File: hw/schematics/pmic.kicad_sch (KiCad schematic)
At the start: 40 parts, among them J1 TYPE-C-31-M-13C, J2 S2B-PH-SM4-TB, U1 NPM1300-QEAA-R

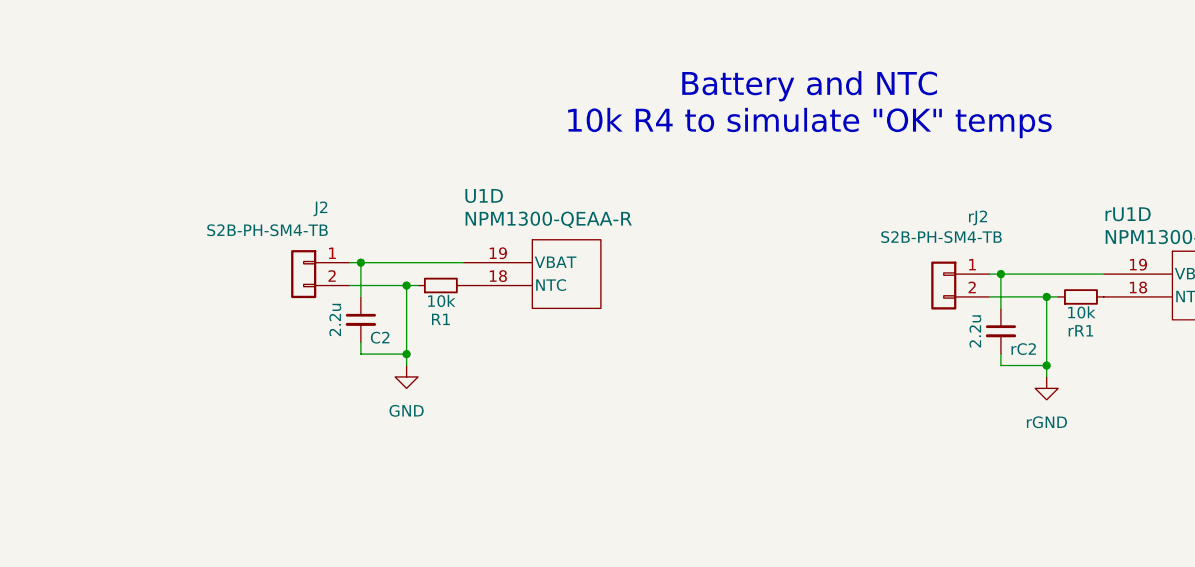
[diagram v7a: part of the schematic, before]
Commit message: Fix missing pads
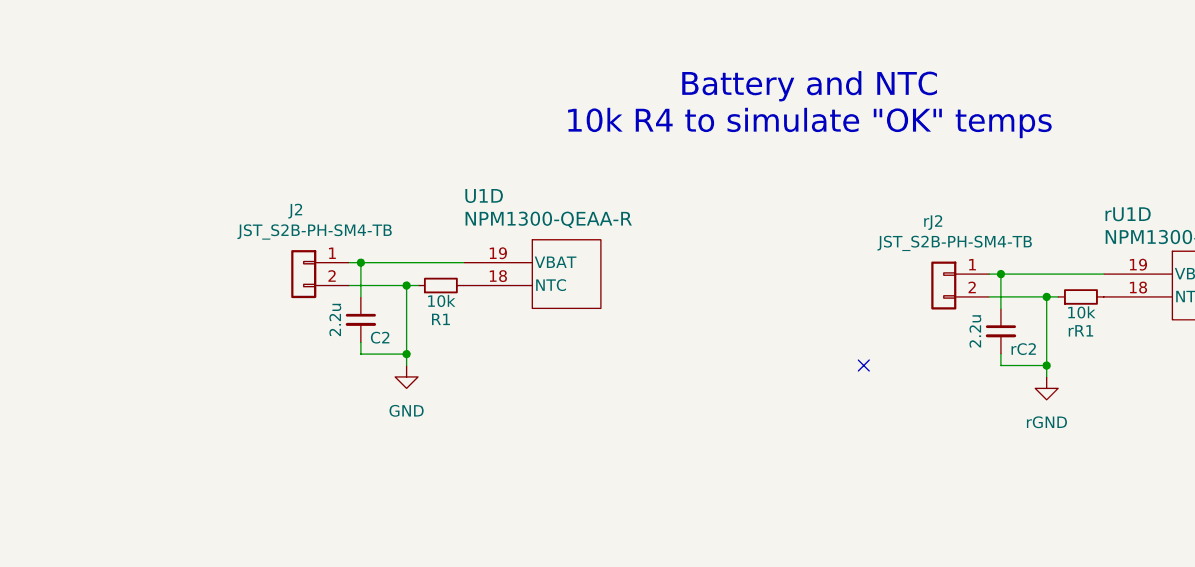
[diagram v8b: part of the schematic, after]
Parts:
- removed J2, rJ2: S2B-PH-SM4-TB, Alidade:JST_S2B-PH-SM4-TB, symbol Alidade:Conn_01x02
- added J2, rJ2: JST_S2B-PH-SM4-TB, Alidade:JST_S2B-PH-SM4-TB, symbol Alidade:JST_S2B-PH-SM4-TB
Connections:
- net GND: now also J2.2 (Pin_2)
- net rGND: now also rJ2.2 (Pin_2)
- net at C2.1, U1.19 (VBAT): now also J2.1 (Pin_1)
- net at rC2.1, rU1.19 (VBAT): now also rJ2.1 (Pin_1)
- no-connect marks 24 -> 25
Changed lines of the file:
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@@
 	)
 	(no_connect
+		(at 332.74 77.47)
+	)
+	(no_connect
 		(at 76.2 67.31)
 	)
@@
 	)
 	(symbol
-		(lib_id "Alidade:Conn_01x02")
-		(at 270.51 66.04 0)
-		(mirror y)
-		(unit 1)
-		(exclude_from_sim no)
-		(in_bom yes)
-		(on_board yes)
-		(dnp no)
-		(property "Reference" "J2"
-			(at 273.304 59.944 0)
-			(effects
-				(font
-					(size 1.27 1.27)
-				)
-				(justify left)
-			)
-		)
-		(property "Value" "S2B-PH-SM4-TB"
-			(at 273.304 62.484 0)
-			(effects
-				(font
-					(size 1.27 1.27)
-				)
-				(justify left)
-			)
-		)
-		(property "Footprint" "Alidade:JST_S2B-PH-SM4-TB"
-			(at 270.51 66.04 0)
-			(effects
-				(font
-					(size 1.27 1.27)
-				)
-				(hide yes)
-			)
-		)
-		(property "Datasheet" "~"
-			(at 270.51 66.04 0)
-			(effects
-				(font
-					(size 1.27 1.27)
-				)
-				(hide yes)
-			)
-		)
-		(property "Description" "Generic connector, single row, 01x02"
-			(at 268.224 58.674 0)
-			(effects
-				(font
-					(size 1.27 1.27)
-				)
-				(hide yes)
-			)
-		)
-		(property "LCSC Part #" "C295747"
-			(at 270.51 66.04 0)
-			(effects
-				(font
-					(size 1.27 1.27)
-				)
-				(hide yes)
-			)
-		)
-		(pin "2"
-		)
-		(pin "1"
-		)
-		(instances
-			(project "alidade"
-				(path "/4cc5d416-57f5-4147-8183-e03ae6b1198a/29a12dcc-0491-44a2-8290-cbef7c573a8c"
-					(reference "J2")
-					(unit 1)
-				)
-			)
-		)
-	)
-	(symbol
 		(lib_id "Alidade:rAVDD")
 		(at 176.53 140.97 0)
@@
 	)
 	(symbol
+		(lib_id "Alidade:JST_S2B-PH-SM4-TB")
+		(at 341.63 67.31 0)
+		(mirror y)
+		(unit 1)
+		(exclude_from_sim no)
+		(in_bom yes)
+		(on_board yes)
+		(dnp no)
+		(property "Reference" "rJ2"
+			(at 341.63 61.468 0)
+			(effects
+				(font
+					(size 1.27 1.27)
+				)
+				(justify left)
+			)
+		)
+		(property "Value" "JST_S2B-PH-SM4-TB"
+			(at 351.536 63.754 0)
+			(effects
+				(font
+					(size 1.27 1.27)
+				)
+				(justify left)
+			)
+		)
+		(property "Footprint" "Alidade:JST_S2B-PH-SM4-TB"
+			(at 341.376 62.992 0)
+			(effects
+				(font
+					(size 1.27 1.27)
+				)
+				(hide yes)
+			)
+		)
+		(property "Datasheet" "~"
+			(at 341.63 67.31 0)
+			(effects
+				(font
+					(size 1.27 1.27)
+				)
+				(hide yes)
+			)
+		)
+		(property "Description" "Generic connector, single row, 01x02"
+			(at 339.344 59.944 0)
+			(effects
+				(font
+					(size 1.27 1.27)
+				)
+				(hide yes)
+			)
+		)
+		(pin "2"
+		)
+		(pin "P2"
+		)
+		(pin "P1"
+		)
+		(pin "1"
+		)
+		(instances
+			(project "alidade"
+				(path "/4cc5d416-57f5-4147-8183-e03ae6b1198a/29a12dcc-0491-44a2-8290-cbef7c573a8c"
+					(reference "rJ2")
+					(unit 1)
+				)
+			)
+		)
+	)
+	(symbol
 		(lib_id "Alidade:rGND")
 		(at 83.82 153.67 0)
@@
 	)
 	(symbol
-		(lib_id "Alidade:Conn_01x02")
-		(at 341.63 67.31 0)
-		(mirror y)
-		(unit 1)
-		(exclude_from_sim no)
-		(in_bom yes)
-		(on_board yes)
-		(dnp no)
-		(property "Reference" "rJ2"
-			(at 345.44 60.96 0)
-			(effects
-				(font
-					(size 1.27 1.27)
-				)
-			)
-		)
-		(property "Value" "S2B-PH-SM4-TB"
-			(at 341.376 63.246 0)
-			(effects
-				(font
-					(size 1.27 1.27)
-				)
-			)
-		)
-		(property "Footprint" "Alidade:JST_S2B-PH-SM4-TB"
-			(at 341.63 67.31 0)
-			(effects
-				(font
-					(size 1.27 1.27)
-				)
-				(hide yes)
-			)
-		)
-		(property "Datasheet" "~"
-			(at 341.63 67.31 0)
-			(effects
-				(font
-					(size 1.27 1.27)
-				)
-				(hide yes)
-			)
-		)
-		(property "Description" "Generic connector, single row, 01x02"
-			(at 339.344 59.944 0)
-			(effects
-				(font
-					(size 1.27 1.27)
-				)
-				(hide yes)
-			)
-		)
-		(property "LCSC Part #" "C295747"
-			(at 341.63 67.31 0)
-			(effects
-				(font
-					(size 1.27 1.27)
-				)
-				(hide yes)
-			)
-		)
-		(pin "1"
-		)
-		(pin "2"
-		)
-		(instances
-			(project "alidade"
-				(path "/4cc5d416-57f5-4147-8183-e03ae6b1198a/29a12dcc-0491-44a2-8290-cbef7c573a8c"
-					(reference "rJ2")
-					(unit 1)
-				)
-			)
-		)
-	)
-	(symbol
 		(lib_id "Alidade:R")
 		(at 250.19 222.25 0)
@@
 					(unit 1)
 				)
+			)
+		)
+	)
+	(symbol
+		(lib_id "Alidade:JST_S2B-PH-SM4-TB")
+		(at 270.51 66.04 0)
+		(mirror y)
+		(unit 1)
+		(exclude_from_sim no)
+		(in_bom yes)
+		(on_board yes)
+		(dnp no)
+		(property "Reference" "J2"
+			(at 270.51 60.198 0)
+			(effects
+				(font
+					(size 1.27 1.27)
+				)
+				(justify left)
+			)
+		)
+		(property "Value" "JST_S2B-PH-SM4-TB"
+			(at 280.416 62.484 0)
+			(effects
+				(font
+					(size 1.27 1.27)
+				)
+				(justify left)
+			)
+		)
+		(property "Footprint" "Alidade:JST_S2B-PH-SM4-TB"
+			(at 270.256 61.722 0)
+			(effects
+				(font
+					(size 1.27 1.27)
+				)
+				(hide yes)
+			)
+		)
+		(property "Datasheet" "~"
+			(at 270.51 66.04 0)
+			(effects
+				(font
+					(size 1.27 1.27)
+				)
+				(hide yes)
+			)
+		)
+		(property "Description" "Generic connector, single row, 01x02"
+			(at 268.224 58.674 0)
+			(effects
+				(font
+					(size 1.27 1.27)
+				)
+				(hide yes)
+			)
+		)
+		(pin "2"
+		)
+		(pin "P2"
+		)
+		(pin "P1"
+		)
+		(pin "1"
+		)
+		(instances
+			(project ""
+				(path "/4cc5d416-57f5-4147-8183-e03ae6b1198a/29a12dcc-0491-44a2-8290-cbef7c573a8c"
+					(reference "J2")
+					(unit 1)
+				)
